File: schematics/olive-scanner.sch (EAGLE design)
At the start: 1 part

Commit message: Adding schematics
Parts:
- added D1, D2, D3, D4, D5, D6: (no value), SparkFun-LED:LED5MM
- added IC1: MCP23008/P, adafruit:MCP23008/P
- added R1, R2, R3, R4, R5, R6: (no value), SparkFun-Resistors:1KOHM-1/4W-5%(PTH)
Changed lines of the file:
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@@
 <layer number="230" name="230bmp" color="7" fill="1" visible="yes" active="yes"/>
 <layer number="231" name="231bmp" color="7" fill="1" visible="yes" active="yes"/>
+<layer number="232" name="Eagle3D_PG2" color="7" fill="1" visible="no" active="no"/>
+<layer number="233" name="Eagle3D_PG3" color="7" fill="1" visible="no" active="no"/>
 <layer number="248" name="Housing" color="7" fill="1" visible="yes" active="yes"/>
 <layer number="249" name="Edge" color="7" fill="1" visible="yes" active="yes"/>
@@
 <parts>
 <part name="U$1" library="SparkFun-DigitalIC" deviceset="ATTINY13" device="DIP"/>
+<part name="IC1" library="adafruit" deviceset="MCP23008" device="/P"/>
+<part name="D1" library="SparkFun-LED" deviceset="LED" device="5MM"/>
+<part name="D2" library="SparkFun-LED" deviceset="LED" device="5MM"/>
+<part name="D3" library="SparkFun-LED" deviceset="LED" device="5MM"/>
+<part name="D4" library="SparkFun-LED" deviceset="LED" device="5MM"/>
+<part name="D5" library="SparkFun-LED" deviceset="LED" device="5MM"/>
+<part name="D6" library="SparkFun-LED" deviceset="LED" device="5MM"/>
+<part name="R1" library="SparkFun-Resistors" deviceset="1KOHM-1/4W-5%(PTH)" device=""/>
+<part name="R2" library="SparkFun-Resistors" deviceset="1KOHM-1/4W-5%(PTH)" device=""/>
+<part name="R3" library="SparkFun-Resistors" deviceset="1KOHM-1/4W-5%(PTH)" device=""/>
+<part name="R4" library="SparkFun-Resistors" deviceset="1KOHM-1/4W-5%(PTH)" device=""/>
+<part name="R5" library="SparkFun-Resistors" deviceset="1KOHM-1/4W-5%(PTH)" device=""/>
+<part name="R6" library="SparkFun-Resistors" deviceset="1KOHM-1/4W-5%(PTH)" device=""/>
 </parts>
 <sheets>
@@
 <instances>
 <instance part="U$1" gate="G$1" x="22.86" y="17.78"/>
+<instance part="IC1" gate="G$1" x="76.2" y="30.48"/>
+<instance part="D1" gate="G$1" x="10.16" y="68.58" rot="R180"/>
+<instance part="D2" gate="G$1" x="20.32" y="68.58" rot="R180"/>
+<instance part="D3" gate="G$1" x="30.48" y="68.58" rot="R180"/>
+<instance part="D4" gate="G$1" x="40.64" y="68.58" rot="R180"/>
+<instance part="D5" gate="G$1" x="50.8" y="68.58" rot="R180"/>
+<instance part="D6" gate="G$1" x="60.96" y="68.58" rot="R180"/>
+<instance part="R1" gate="G$1" x="10.16" y="58.42" rot="R90"/>
+<instance part="R2" gate="G$1" x="20.32" y="58.42" rot="R90"/>
+<instance part="R3" gate="G$1" x="30.48" y="58.42" rot="R90"/>
+<instance part="R4" gate="G$1" x="40.64" y="58.42" rot="R90"/>
+<instance part="R5" gate="G$1" x="50.8" y="58.42" rot="R90"/>
+<instance part="R6" gate="G$1" x="60.96" y="58.42" rot="R90"/>
 </instances>
 <busses>

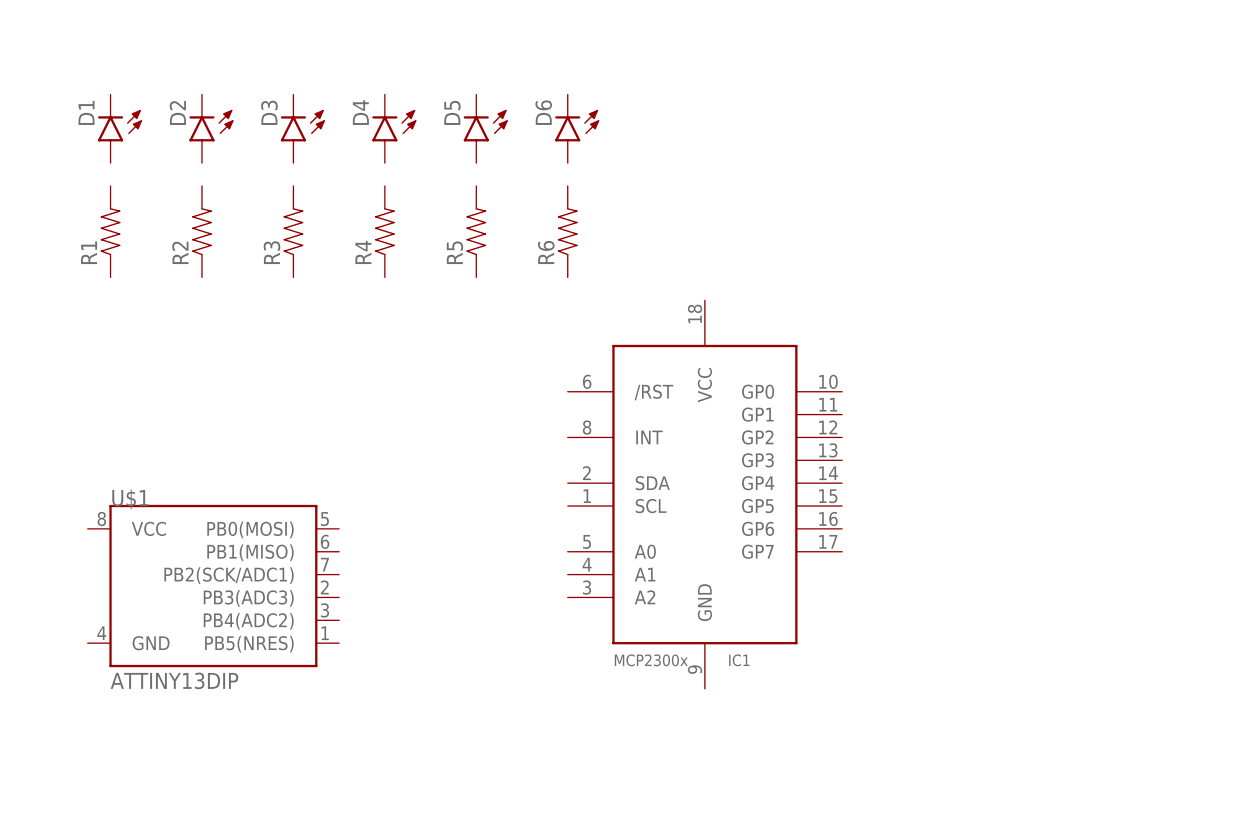
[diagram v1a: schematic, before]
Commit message: Did the schematics and updated the docs
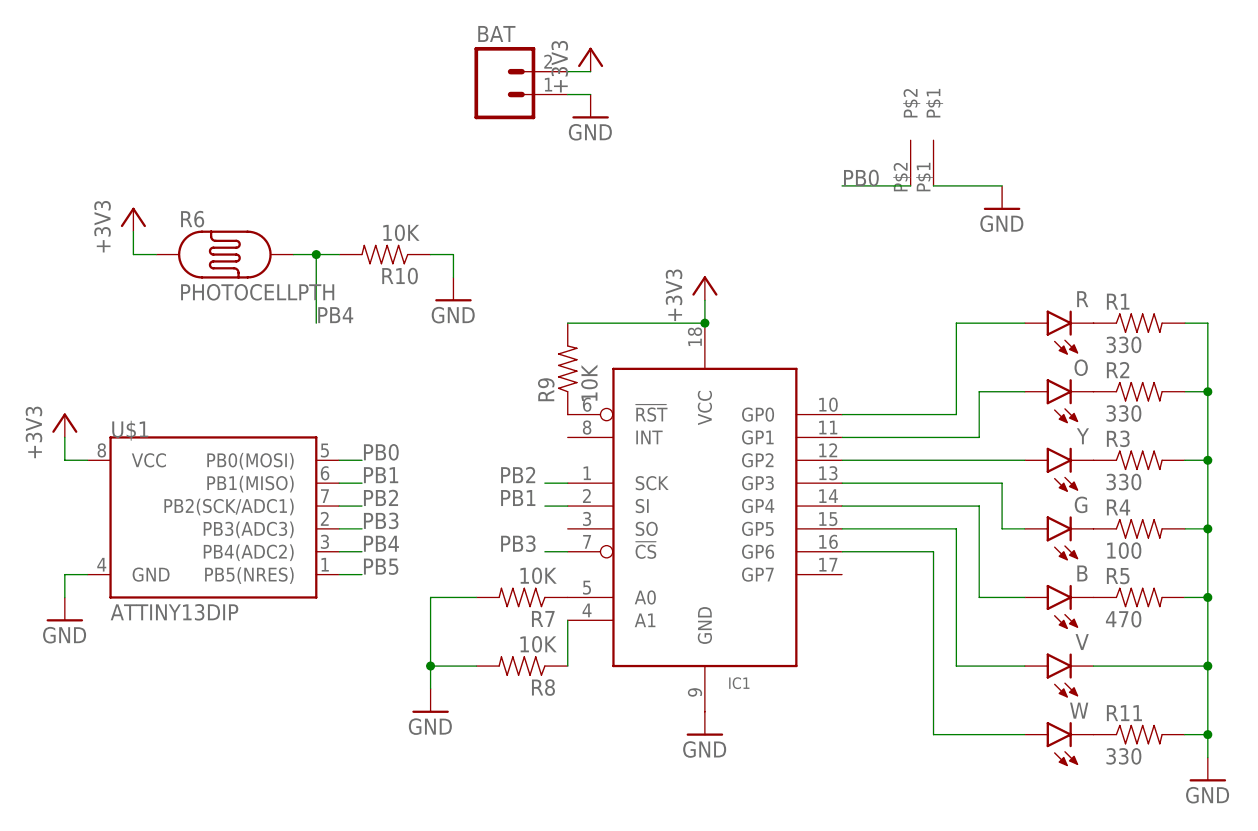
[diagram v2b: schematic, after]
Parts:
- removed D1, D2, D3, D4, D5, D6: (no value), SparkFun-LED:LED5MM
- added B, G, O, R, V, W, Y: (no value), SparkFun-LED:LED5MM
- added BAT: (no value), SparkFun-Connectors:M02LOCK
- added R10, R7, R8, R9: 10K, SparkFun-Resistors:1KOHM-1/4W-5%(PTH)
- added R11: 330, SparkFun-Resistors:1KOHM-1/4W-5%(PTH)
- added U$2: PHONE_VIBRATOR, HokieGeek:PHONE_VIBRATOR
- IC1: value MCP23008/P -> MCP23S08/P; device adafruit:MCP23008/P -> HokieGeek:MCP23S08/P
- R1, R2, R3: value (none) -> 330
- R4: value (none) -> 100
- R5: value (none) -> 470
- R6: value (none) -> PHOTOCELLPTH; device SparkFun-Resistors:1KOHM-1/4W-5%(PTH) -> SparkFun-Sensors:PHOTOCELLPTH
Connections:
- new net +3V3: BAT.2, IC1.VCC, R6.P$1, R9.2, U$1.VCC
- new net GND: BAT.1, IC1.GND, R1.2, R10.1, R11.2, R2.2, R3.2, R4.2, R5.2, R7.2, R8.2, U$1.GND, U$2.P$1, V.C
- new net N$1: IC1.A1, R8.1
- new net N$10: IC1.GP6, W.A
- new net N$19: IC1.GP0, R.A
- new net N$2: IC1.!RST, R9.1
- new net N$20: IC1.GP1, O.A
- new net N$21: IC1.GP2, Y.A
- new net N$22: G.A, IC1.GP3
- new net N$23: B.A, IC1.GP4
- new net N$24: IC1.GP5, V.A
- new net N$3: IC1.A0, R7.1
- new net N$4: R.C, R1.1
- new net N$5: O.C, R2.1
- new net N$6: R3.1, Y.C
- new net N$7: G.C, R4.1
- new net N$8: B.C, R5.1
- new net N$9: R11.1, W.C
- new net PB0: U$1.PB0(MOSI), U$2.P$2
- new net PB1: IC1.SI, U$1.PB1(MISO)
- new net PB2: IC1.SCK, U$1.PB2(SCK/ADC1)
- new net PB3: IC1.!CS, U$1.PB3(ADC3)
- new net PB4: R10.2, R6.P$2, U$1.PB4(ADC2)
- new net PB5: U$1.PB5(NRES)
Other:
- moved on the sheet: R1, R2, R3, R4, R5, U$1
